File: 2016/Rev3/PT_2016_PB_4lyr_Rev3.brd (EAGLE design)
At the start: 155.7 x 202.7 mm, 166 parts, among them Q1 MOSFET-NCHANNELFDD8780, Q12 2N7002, Q2 MMBT2222A, Q3 MOSFET-NCHANNELFDD8780, Q4 MMBT2222A

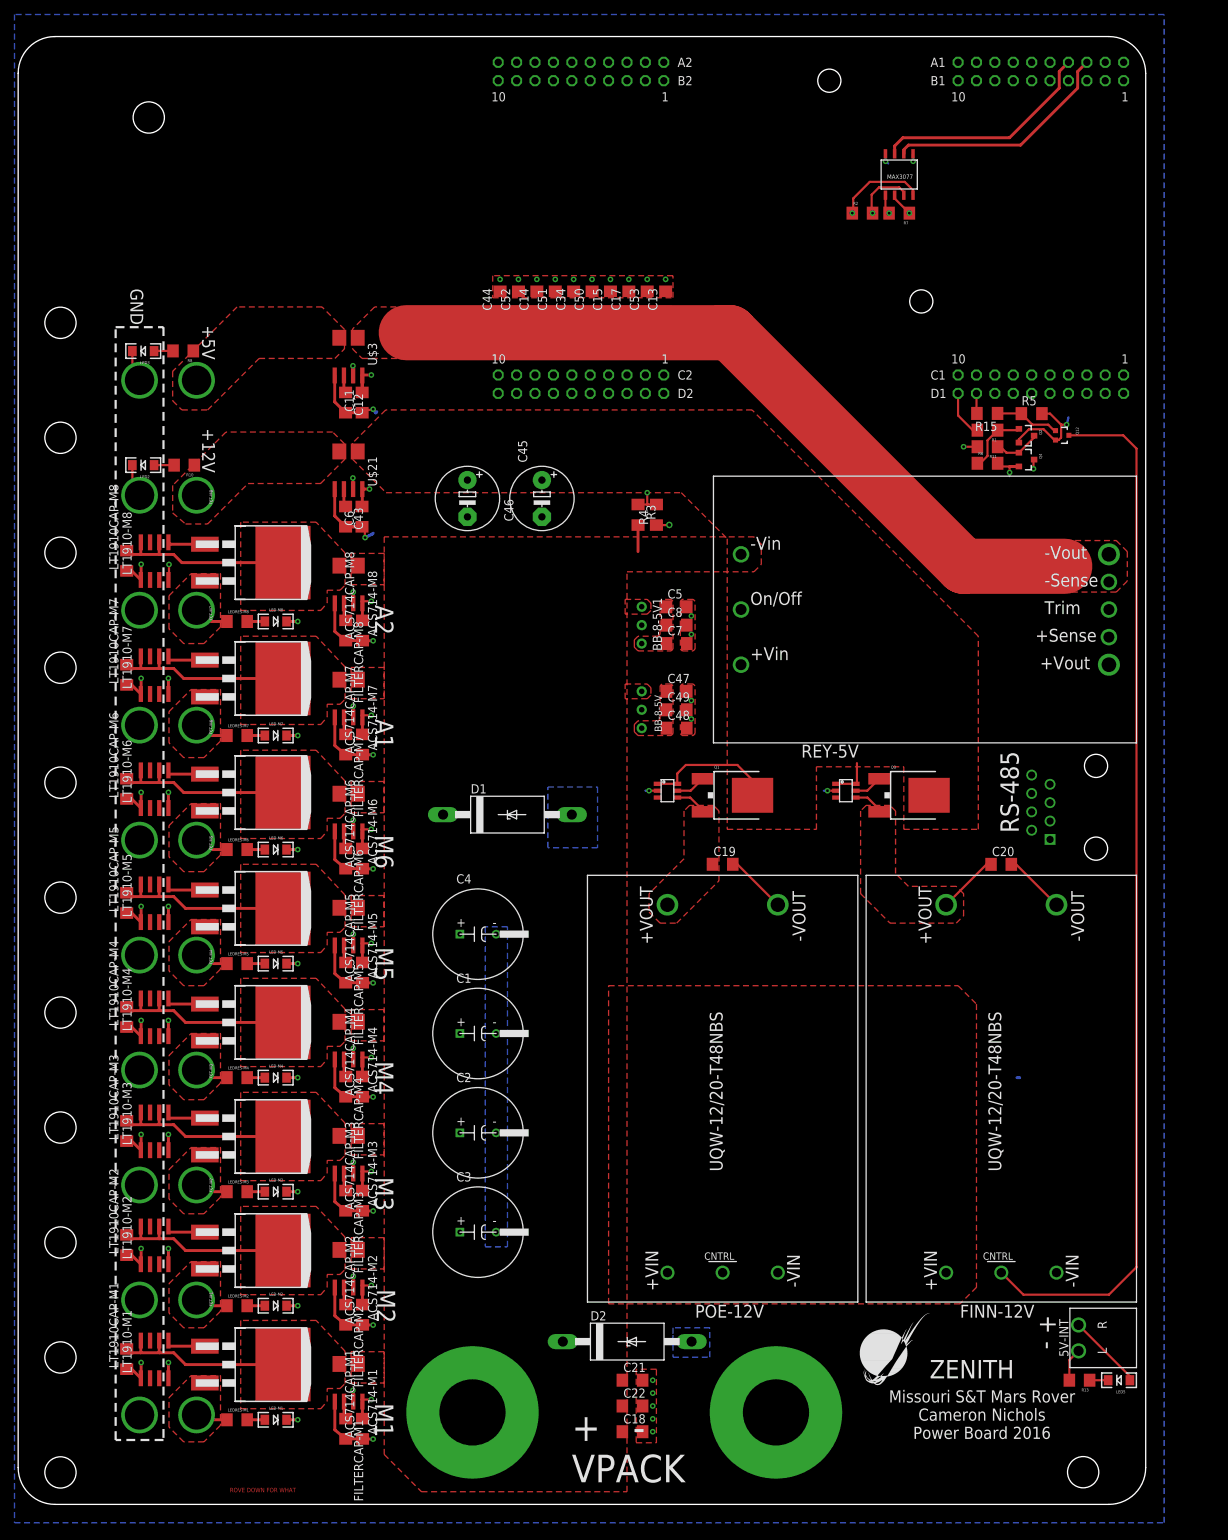
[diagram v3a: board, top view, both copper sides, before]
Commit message: Moved tiva and enlarged board .25 in to right
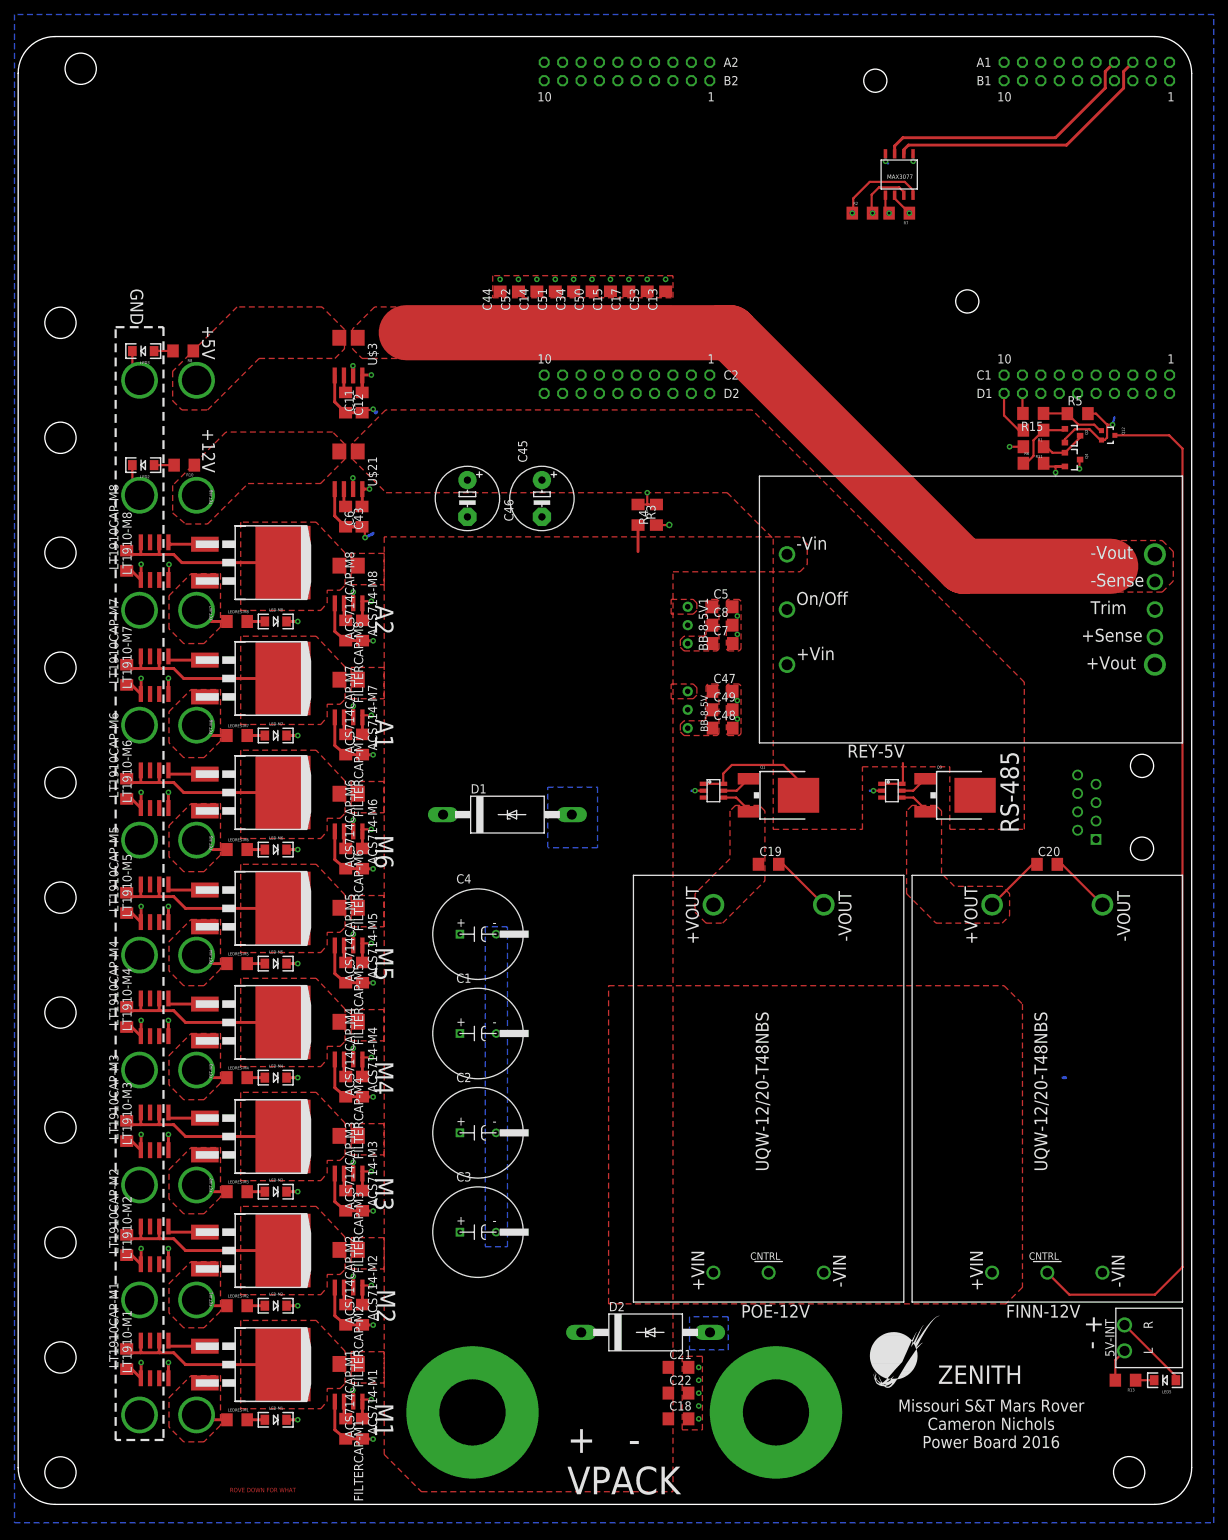
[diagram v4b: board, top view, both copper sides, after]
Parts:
- moved U$10 11.6 mm to (8.64, 198.2)
- moved C18 6.59 mm to (91.2, 11.8)
- moved C21 6.59 mm to (91.2, 18.9)
- moved C22 6.59 mm to (91.2, 15.4)
- moved R15 6.35 mm to (140.2, 150.6)
- moved BB-8-5V 6.35 mm to (92.5, 112.3)
- moved BB-8-5V1 6.35 mm to (92.5, 124.0)
- moved C19 6.35 mm to (103.6, 88.4)
- moved POE-12V 6.35 mm to (103.6, 57.4)
- moved Q3 6.35 mm to (130.6, 97.9)
- moved U$6 6.35 mm to (120.7, 98.6)
- moved U$1 6.35 mm to (35.8, 144.5)
- moved 5V-INT 6.35 mm to (152.8, 23.0)
- moved C20 6.35 mm to (142.1, 88.4)
- moved C47 6.35 mm to (97.3, 112.3)
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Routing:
- net VMEAS-VBATT: track 197.3 -> 203.6 mm
- net SIG-M5: track 133.0 -> 139.4 mm
- net SIG-M4: track 149.7 -> 156.0 mm
- net SIG-M2: track 177.0 -> 183.3 mm
- net SIG-M1: track 187.7 -> 194.1 mm
- net IMEAS-M7: track 138.3 -> 144.7 mm
- net IMEAS-M3: track 204.7 -> 211.1 mm
- net IMEAS-M1: track 238.8 -> 245.1 mm
- net IMEAS-12V: track 153.0 -> 159.4 mm
- net SIG-M7: track 114.7 -> 121.0 mm
- net REC+1: track 122.1 -> 128.4 mm
- net TRANS-1: track 99.0 -> 105.4 mm
- net TRANS+1: track 104.5 -> 110.9 mm
- net SIG-M8: track 101.4 -> 107.8 mm
- net SIG-M6: track 120.2 -> 126.5 mm
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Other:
- board size 155.7 x 202.7 mm -> 162.1 x 202.7 mm

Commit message: Improved some top planes
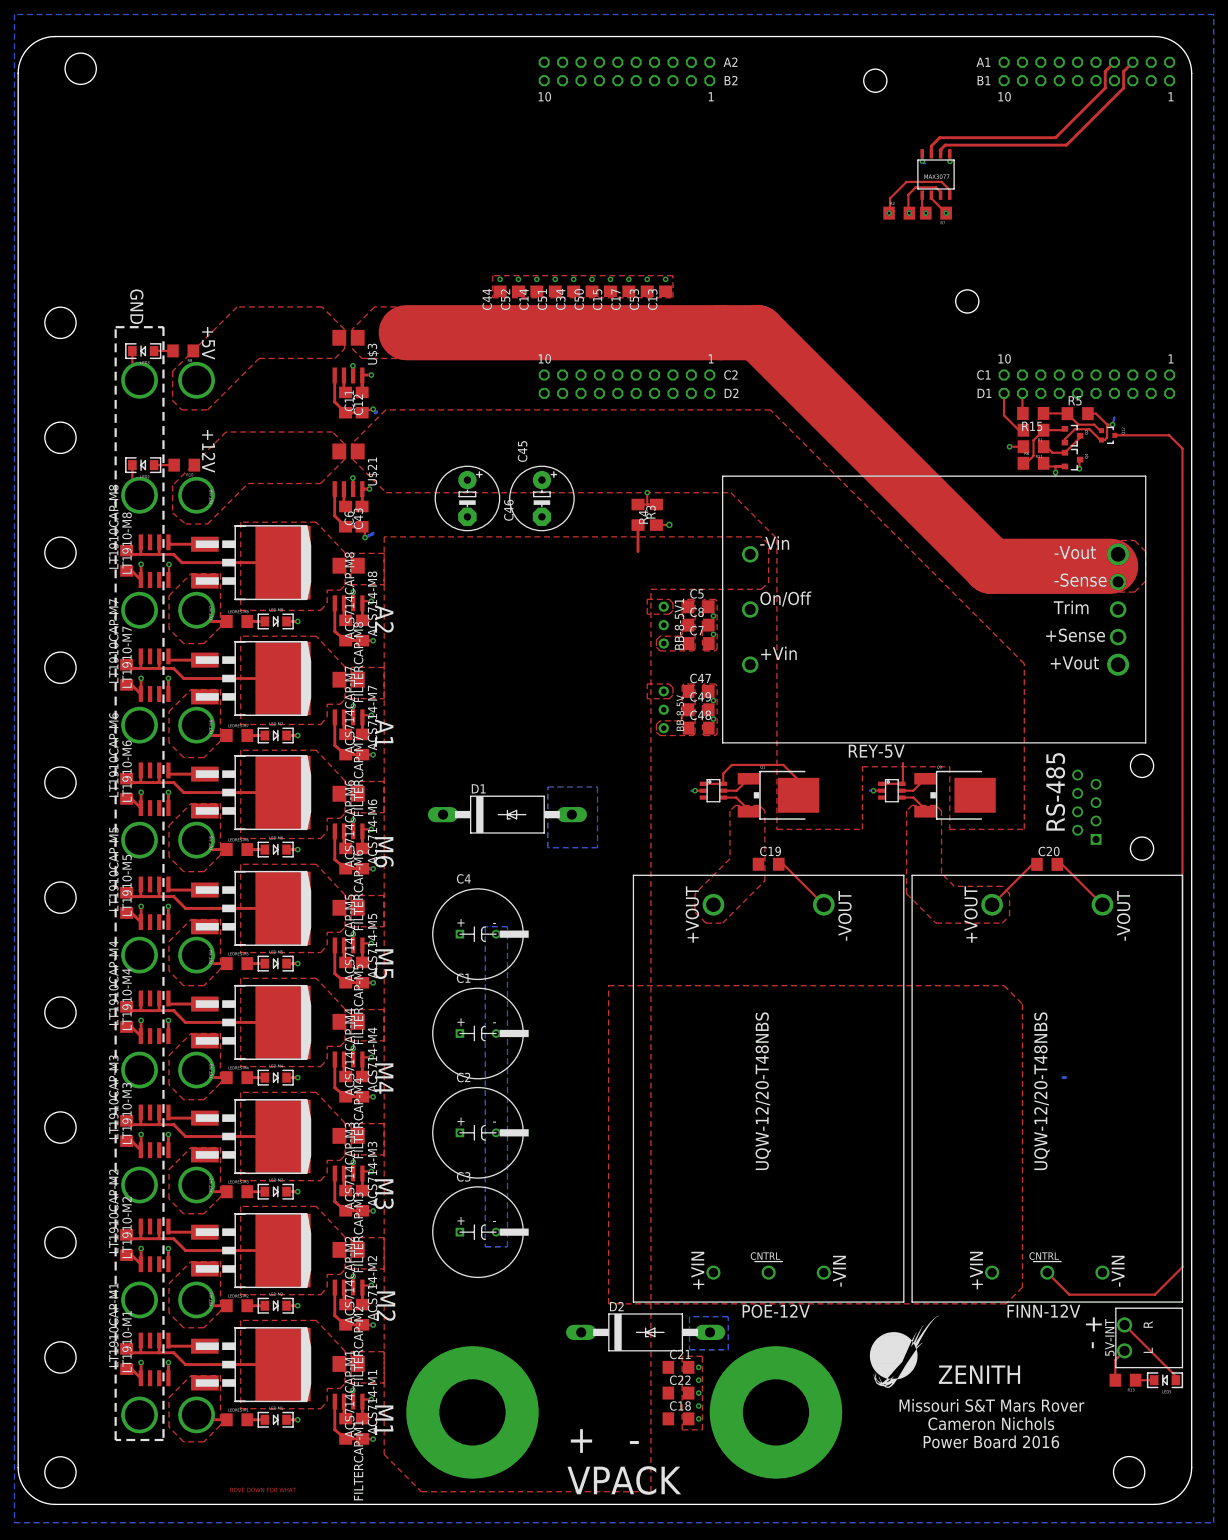
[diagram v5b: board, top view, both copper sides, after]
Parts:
- moved R2 5.08 mm to (121.7, 178.3)
- moved R7 5.08 mm to (126.7, 178.3)
- moved U$24 5.08 mm to (126.7, 183.6)
- moved U$7 5.08 mm to (125.2, 124.2)
- moved BB-8-5V 3.30 mm to (89.2, 112.3)
- moved BB-8-5V1 3.30 mm to (89.2, 124.0)
- moved C47 3.30 mm to (94.0, 112.3)
- moved C48 3.30 mm to (94.0, 107.2)
- moved C49 3.30 mm to (94.0, 109.7)
- moved C5 3.30 mm to (94.0, 124.0)
- moved C7 3.30 mm to (94.0, 118.9)
- moved C8 3.30 mm to (94.0, 121.4)
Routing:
- net TRANS-1: track 105.4 -> 100.3 mm
- net REC-1: track 118.6 -> 113.5 mm
- net V_BATT: track 42.4 -> 47.5 mm
- net TRANS+1: track 110.9 -> 105.8 mm
- net RX1: track 38.5 -> 33.5 mm
- net REC+1: track 128.4 -> 123.4 mm
- net N$11: track 49.7 -> 54.8 mm
- net TX1: track 37.6 -> 32.5 mm
- net 5V: track 335.9 -> 337.8 mm

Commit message: Fixed an issue and gen DXF
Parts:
- moved C18 3.30 mm to (87.9, 11.8)
- moved C21 3.30 mm to (87.9, 18.9)
- moved C22 3.30 mm to (87.9, 15.4)
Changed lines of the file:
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@@
 <?xml version="1.0" encoding="utf-8"?>
 <!DOCTYPE eagle SYSTEM "eagle.dtd">
-<eagle version="7.3.0">
+<eagle version="7.4.0">
 <drawing>
 <settings>
@@
 <element name="C15" library="resistor" package="C1206" value="1uF" x="81.788" y="166.116" rot="R90"/>
 <element name="C17" library="resistor" package="C1206" value="1uF" x="84.328" y="166.116" rot="R90"/>
-<element name="C18" library="resistor" package="C1206" value="1nF" x="91.186" y="11.811"/>
-<element name="C21" library="resistor" package="C1206" value="10uF" x="91.186" y="18.923"/>
-<element name="C22" library="resistor" package="C1206" value=".1uF" x="91.186" y="15.367"/>
+<element name="C18" library="resistor" package="C1206" value="1nF" x="87.884" y="11.811"/>
+<element name="C21" library="resistor" package="C1206" value="10uF" x="87.884" y="18.923"/>
+<element name="C22" library="resistor" package="C1206" value=".1uF" x="87.884" y="15.367"/>
 <element name="C34" library="resistor" package="C1206" value="1uF" x="76.708" y="166.116" rot="R90"/>
 <element name="C44" library="resistor" package="C1206" value="1uF" x="66.548" y="166.116" rot="R90"/>
@@
 <wire x1="16.9799" y1="17.4533" x2="16.9418" y2="17.4152" width="0.4064" layer="1"/>
 <polygon width="0.4064" layer="1" thermals="no">
-<vertex x="91.694" y="20.447"/>
-<vertex x="91.694" y="10.287"/>
-<vertex x="94.488" y="10.287"/>
-<vertex x="94.488" y="20.447"/>
-</polygon>
-<via x="93.98" y="11.811" extent="1-16" drill="0.381"/>
-<via x="93.98" y="13.589" extent="1-16" drill="0.381"/>
-<via x="93.98" y="15.367" extent="1-16" drill="0.381"/>
-<via x="93.98" y="17.145" extent="1-16" drill="0.381"/>
-<via x="93.98" y="18.923" extent="1-16" drill="0.381"/>
+<vertex x="88.392" y="20.447"/>
+<vertex x="88.392" y="10.287"/>
+<vertex x="91.186" y="10.287"/>
+<vertex x="91.186" y="20.447"/>
+</polygon>
+<via x="90.678" y="11.811" extent="1-16" drill="0.381"/>
+<via x="90.678" y="13.589" extent="1-16" drill="0.381"/>
+<via x="90.678" y="15.367" extent="1-16" drill="0.381"/>
+<via x="90.678" y="17.145" extent="1-16" drill="0.381"/>
+<via x="90.678" y="18.923" extent="1-16" drill="0.381"/>
 <contactref element="LT1910-M2" pad="1"/>
 <contactref element="LT1910CAP-M2" pad="1"/>
@@
 <wire x1="136.906" y1="146.05" x2="122.047" y2="131.191" width="0.3048" layer="2"/>
 <wire x1="122.047" y1="131.191" x2="101.092" y2="131.191" width="0.3048" layer="2"/>
-<wire x1="89.786" y1="15.367" x2="89.786" y2="18.923" width="0" layer="19" extent="1-1"/>
-<wire x1="89.786" y1="11.811" x2="89.786" y2="15.367" width="0" layer="19" extent="1-1"/>
-<wire x1="77.75575" y1="23.749" x2="89.786" y2="18.923" width="0" layer="19" extent="1-1"/>
 </signal>
 <signal name="N$4">
@@
 <contactref element="U$26" pad="P$2"/>
 <polygon width="0.508" layer="1" thermals="no">
-<vertex x="31.75" y="140.97"/>
-<vertex x="41.7576" y="140.97"/>
+<vertex x="30.48" y="139.7"/>
+<vertex x="40.4876" y="139.7"/>
 <vertex x="45.0596" y="144.272"/>
 <vertex x="45.0596" y="146.4564"/>
-<vertex x="43.434" y="148.082"/>
-<vertex x="28.702" y="148.082"/>
+<vertex x="40.386" y="151.13"/>
+<vertex x="31.75" y="151.13"/>
 <vertex x="21.336" y="140.716"/>
 <vertex x="21.336" y="136.906"/>
